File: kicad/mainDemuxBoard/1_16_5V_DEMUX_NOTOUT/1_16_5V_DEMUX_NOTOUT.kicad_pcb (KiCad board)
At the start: 4 copper layers, 168 parts, among them Q1 PMOS, Q10 PMOS, Q100 PMOS, Q101 PMOS, Q102 PMOS, Q103 PMOS, Q104 NMOS, Q105 NMOS, Q106 NMOS, Q107 NMOS, Q108 NMOS, Q109 PMOS, Q11 PMOS, Q110 PMOS, Q111 PMOS, Q112 PMOS, Q113 PMOS, Q114 NMOS, Q115 NMOS, Q116 NMOS, Q117 NMOS, Q118 NMOS, Q119 PMOS, Q12 PMOS, Q120 PMOS, Q121 PMOS, Q122 PMOS, Q123 PMOS, Q124 NMOS, Q125 NMOS, Q126 NMOS, Q127 NMOS, Q128 NMOS, Q129 PMOS, Q13 PMOS, Q130 PMOS, Q131 PMOS, Q132 PMOS, Q133 PMOS, Q134 NMOS, Q135 NMOS, Q136 NMOS, Q137 NMOS, Q138 NMOS, Q139 PMOS, Q14 NMOS, Q140 PMOS, Q141 PMOS, Q142 PMOS, Q143 PMOS, Q144 NMOS, Q145 NMOS, Q146 NMOS, Q147 NMOS, Q148 NMOS, Q149 PMOS, Q15 NMOS, Q150 PMOS, Q151 PMOS, Q152 PMOS, Q153 PMOS, Q154 NMOS, Q155 NMOS, Q156 NMOS, Q157 NMOS, Q158 NMOS, Q159 PMOS, Q16 NMOS, Q160 PMOS, Q161 PMOS, Q162 PMOS, Q163 PMOS, Q164 NMOS, Q165 NMOS, Q166 NMOS, Q167 NMOS, Q168 NMOS, Q17 NMOS, Q18 NMOS, Q19 PMOS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

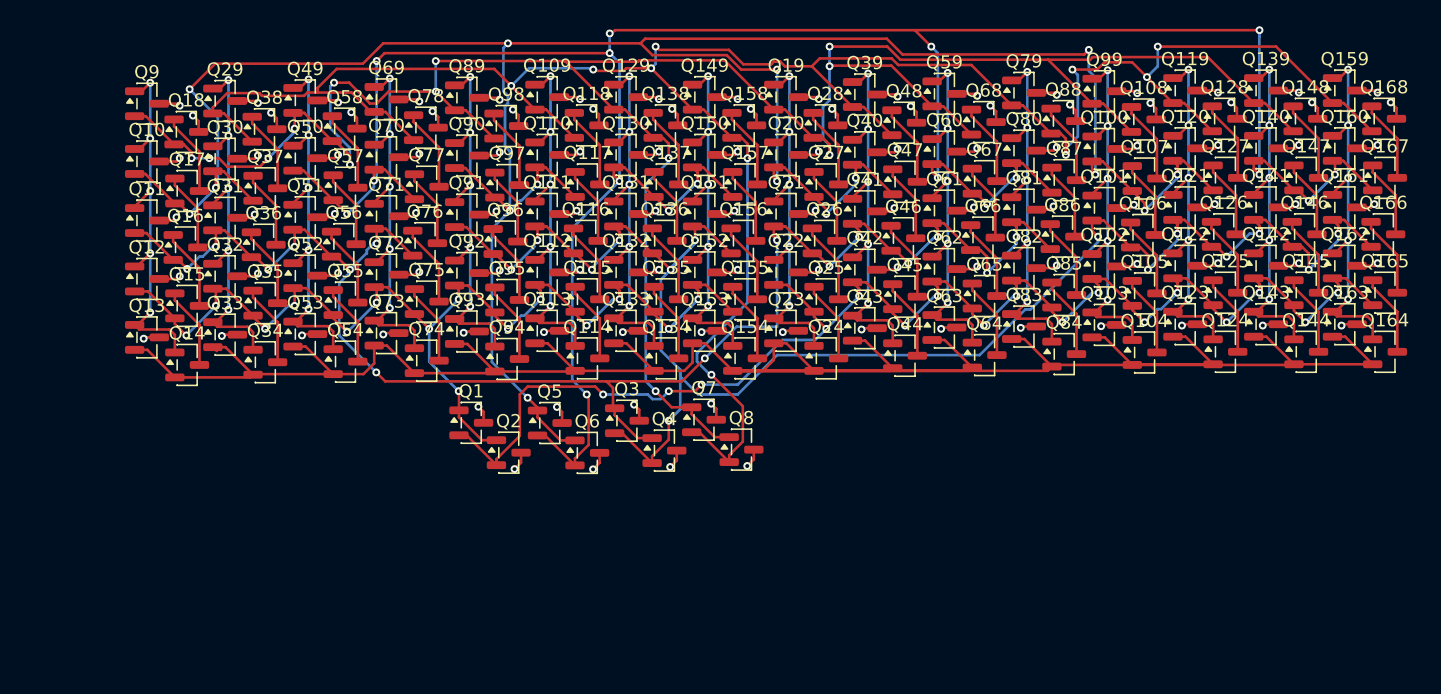
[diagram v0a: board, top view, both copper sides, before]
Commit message: update main board schematic
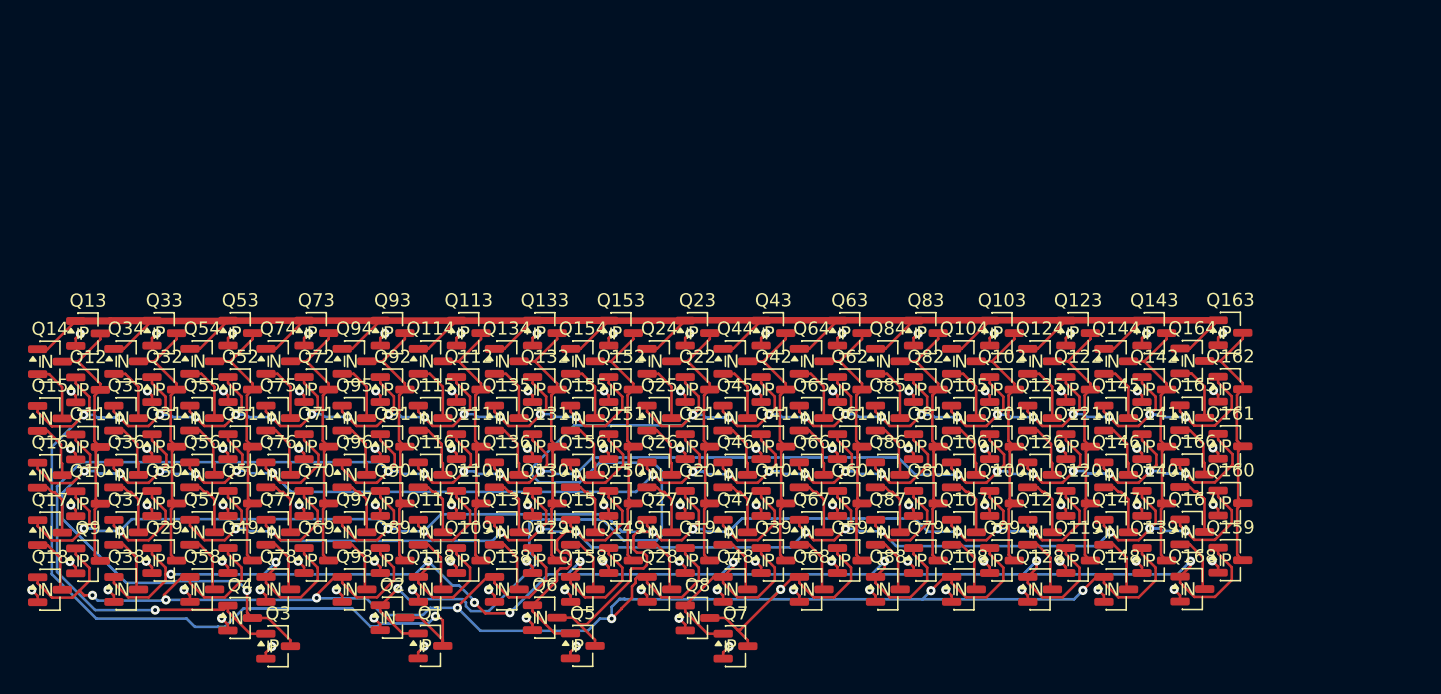
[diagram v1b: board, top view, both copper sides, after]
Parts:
- Q1, Q10, Q100, Q101, Q102, Q103, Q109, Q11, Q110, Q111, Q112, Q113, Q119, Q12, Q120, Q121, Q122, Q123, Q129, Q13, Q130, Q131, Q132, Q133, Q139, Q140, Q141, Q142, Q143, Q149, Q150, Q151, Q152, Q153, Q159, Q160, Q161, Q162, Q163, Q19, Q20, Q21, Q22, Q23, Q29, Q3, Q30, Q31, Q32, Q33, Q39, Q40, Q41, Q42, Q43, Q49, Q5, Q50, Q51, Q52, Q53, Q59, Q60, Q61, Q62, Q63, Q69, Q7, Q70, Q71, Q72, Q73, Q79, Q80, Q81, Q82, Q83, Q89, Q9, Q90, Q91, Q92, Q93, Q99: value PMOS -> Q_PMOS_GSD; footprint Package_TO_SOT_SMD:SOT-23 -> easyeda2kicad:SOT-23-P
- Q104, Q105, Q106, Q107, Q108, Q114, Q115, Q116, Q117, Q118, Q124, Q125, Q126, Q127, Q128, Q134, Q135, Q136, Q137, Q138, Q14, Q144, Q145, Q146, Q147, Q148, Q15, Q154, Q155, Q156, Q157, Q158, Q16, Q164, Q165, Q166, Q167, Q168, Q17, Q18, Q2, Q24, Q25, Q26, Q27, Q28, Q34, Q35, Q36, Q37, Q38, Q4, Q44, Q45, Q46, Q47, Q48, Q54, Q55, Q56, Q57, Q58, Q6, Q64, Q65, Q66, Q67, Q68, Q74, Q75, Q76, Q77, Q78, Q8, Q84, Q85, Q86, Q87, Q88, Q94, Q95, Q96, Q97, Q98: value NMOS -> Q_NMOS_GSD; footprint Package_TO_SOT_SMD:SOT-23 -> easyeda2kicad:SOT-23-N
- moved Q168 38.7 mm to (121.2, 128.8)
- moved Q148 38.6 mm to (115.4, 128.8)
- moved Q128 38.5 mm to (109.6, 128.8)
- moved Q108 38.3 mm to (103.8, 128.8)
- moved Q88 38.1 mm to (98.0, 128.8)
- moved Q68 37.9 mm to (92.2, 128.8)
- moved Q48 37.8 mm to (86.4, 128.8)
- moved Q28 37.5 mm to (80.6, 128.8)
- moved Q158 37.4 mm to (74.8, 128.8)
- moved Q138 37.3 mm to (69.0, 128.8)
- moved Q118 37.3 mm to (63.2, 128.8)
- moved Q98 37.1 mm to (57.4, 128.8)
- moved Q78 36.9 mm to (51.6, 128.8)
- moved Q159 36.8 mm to (124.1, 126.6)
- moved Q139 36.8 mm to (118.3, 126.7)
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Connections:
- Q1 pad 1: /5VNOT/Y -> /S_{0}
- Q1 pad 2: /S_{0} -> +5V
- Q1 pad 3: +5V -> /5VNOT/Y
- Q10 pad 1: /~{Y_{0}} -> /5VNOT2/Y
- Q10 pad 2: /5VNOT2/Y -> +5V
- Q10 pad 3: +5V -> /~{Y_{0}}
- Q100 pad 1: /~{Y_{12}} -> /5VNOT2/Y
- Q100 pad 2: /5VNOT2/Y -> +5V
- Q100 pad 3: +5V -> /~{Y_{12}}
- Q101 pad 1: /~{Y_{12}} -> /S_{1}
- Q101 pad 2: /S_{1} -> +5V
- Q101 pad 3: +5V -> /~{Y_{12}}
- Q102 pad 1: /~{Y_{12}} -> /S_{0}
- Q102 pad 2: /S_{0} -> +5V
- Q102 pad 3: +5V -> /~{Y_{12}}
- Q103 pad 1: /~{Y_{12}} -> /D
- Q103 pad 2: /D -> +5V
- Q103 pad 3: +5V -> /~{Y_{12}}
- Q104 pad 1: /~{Y_{12}} -> /D
- Q104 pad 2: /D -> Net-(Q104-S)
- Q104 pad 3: Net-(Q104-S) -> /~{Y_{12}}
- Q105 pad 1: Net-(Q104-S) -> /S_{0}
- Q105 pad 2: /S_{0} -> Net-(Q105-S)
- Q105 pad 3: Net-(Q105-S) -> Net-(Q104-S)
- Q106 pad 1: Net-(Q105-S) -> /S_{1}
- Q106 pad 2: /S_{1} -> Net-(Q106-S)
- Q106 pad 3: Net-(Q106-S) -> Net-(Q105-S)
- Q107 pad 1: Net-(Q106-S) -> /5VNOT2/Y
- Q107 pad 2: /5VNOT2/Y -> Net-(Q107-S)
- Q107 pad 3: Net-(Q107-S) -> Net-(Q106-S)
- Q108 pad 1: Net-(Q107-S) -> /5VNOT3/Y
- Q108 pad 2: /5VNOT3/Y -> GND
- Q108 pad 3: GND -> Net-(Q107-S)
- Q109 pad 1: /~{Y_{5}} -> /S_{3}
- Q109 pad 2: /S_{3} -> +5V
- Q109 pad 3: +5V -> /~{Y_{5}}
- Q11 pad 1: /~{Y_{0}} -> /5VNOT1/Y
- Q11 pad 2: /5VNOT1/Y -> +5V
- Q11 pad 3: +5V -> /~{Y_{0}}
- Q110 pad 1: /~{Y_{5}} -> /5VNOT2/Y
- Q110 pad 2: /5VNOT2/Y -> +5V
- Q110 pad 3: +5V -> /~{Y_{5}}
- Q111 pad 1: /~{Y_{5}} -> /S_{1}
- Q111 pad 2: /S_{1} -> +5V
- Q111 pad 3: +5V -> /~{Y_{5}}
- Q112 pad 1: /~{Y_{5}} -> /5VNOT/Y
- Q112 pad 2: /5VNOT/Y -> +5V
- Q112 pad 3: +5V -> /~{Y_{5}}
- Q113 pad 1: /~{Y_{5}} -> /D
- Q113 pad 2: /D -> +5V
- Q113 pad 3: +5V -> /~{Y_{5}}
- Q114 pad 1: /~{Y_{5}} -> /D
- Q114 pad 2: /D -> Net-(Q114-S)
- Q114 pad 3: Net-(Q114-S) -> /~{Y_{5}}
- Q115 pad 1: Net-(Q114-S) -> /5VNOT/Y
- Q115 pad 2: /5VNOT/Y -> Net-(Q115-S)
- Q115 pad 3: Net-(Q115-S) -> Net-(Q114-S)
- Q116 pad 1: Net-(Q115-S) -> /S_{1}
- Q116 pad 2: /S_{1} -> Net-(Q116-S)
- Q116 pad 3: Net-(Q116-S) -> Net-(Q115-S)
- Q117 pad 1: Net-(Q116-S) -> /5VNOT2/Y
- Q117 pad 2: /5VNOT2/Y -> Net-(Q117-S)
- Q117 pad 3: Net-(Q117-S) -> Net-(Q116-S)
- Q118 pad 1: Net-(Q117-S) -> /S_{3}
- Q118 pad 2: /S_{3} -> GND
- Q118 pad 3: GND -> Net-(Q117-S)
- Q119 pad 1: /~{Y_{13}} -> /S_{3}
- Q119 pad 2: /S_{3} -> +5V
- Q119 pad 3: +5V -> /~{Y_{13}}
- Q12 pad 1: /~{Y_{0}} -> /5VNOT/Y
- Q12 pad 2: /5VNOT/Y -> +5V
- Q12 pad 3: +5V -> /~{Y_{0}}
- Q120 pad 1: /~{Y_{13}} -> /5VNOT2/Y
- Q120 pad 2: /5VNOT2/Y -> +5V
- Q120 pad 3: +5V -> /~{Y_{13}}
- Q121 pad 1: /~{Y_{13}} -> /S_{1}
- Q121 pad 2: /S_{1} -> +5V
- Q121 pad 3: +5V -> /~{Y_{13}}
- Q122 pad 1: /~{Y_{13}} -> /S_{0}
- Q122 pad 2: /S_{0} -> +5V
- Q122 pad 3: +5V -> /~{Y_{13}}
- Q123 pad 1: /~{Y_{13}} -> /D
- Q123 pad 2: /D -> +5V
- Q123 pad 3: +5V -> /~{Y_{13}}
- Q124 pad 1: /~{Y_{13}} -> /D
- Q124 pad 2: /D -> Net-(Q124-S)
- Q124 pad 3: Net-(Q124-S) -> /~{Y_{13}}
- Q125 pad 1: Net-(Q124-S) -> /S_{0}
- Q125 pad 2: /S_{0} -> Net-(Q125-S)
- Q125 pad 3: Net-(Q125-S) -> Net-(Q124-S)
- Q126 pad 1: Net-(Q125-S) -> /S_{1}
- Q126 pad 2: /S_{1} -> Net-(Q126-S)
- Q126 pad 3: Net-(Q126-S) -> Net-(Q125-S)
- Q127 pad 1: Net-(Q126-S) -> /5VNOT2/Y
- Q127 pad 2: /5VNOT2/Y -> Net-(Q127-S)
- Q127 pad 3: Net-(Q127-S) -> Net-(Q126-S)
- Q128 pad 1: Net-(Q127-S) -> /S_{3}
- Q128 pad 2: /S_{3} -> GND
- Q128 pad 3: GND -> Net-(Q127-S)
- Q129 pad 1: /~{Y_{6}} -> /5VNOT3/Y
- Q129 pad 2: /5VNOT3/Y -> +5V
- Q129 pad 3: +5V -> /~{Y_{6}}
- Q13 pad 1: /~{Y_{0}} -> /D
- Q13 pad 2: /D -> +5V
- Q13 pad 3: +5V -> /~{Y_{0}}
- Q130 pad 1: /~{Y_{6}} -> /S_{2}
- Q130 pad 2: /S_{2} -> +5V
- Q130 pad 3: +5V -> /~{Y_{6}}
- Q131 pad 1: /~{Y_{6}} -> /S_{1}
- Q131 pad 2: /S_{1} -> +5V
- Q131 pad 3: +5V -> /~{Y_{6}}
- Q132 pad 1: /~{Y_{6}} -> /5VNOT/Y
- Q132 pad 2: /5VNOT/Y -> +5V
- Q132 pad 3: +5V -> /~{Y_{6}}
- Q133 pad 1: /~{Y_{6}} -> /D
- Q133 pad 2: /D -> +5V
- Q133 pad 3: +5V -> /~{Y_{6}}
- Q134 pad 1: /~{Y_{6}} -> /D
- Q134 pad 2: /D -> Net-(Q134-S)
- Q134 pad 3: Net-(Q134-S) -> /~{Y_{6}}
- Q135 pad 1: Net-(Q134-S) -> /5VNOT/Y
- Q135 pad 2: /5VNOT/Y -> Net-(Q135-S)
- Q135 pad 3: Net-(Q135-S) -> Net-(Q134-S)
- Q136 pad 1: Net-(Q135-S) -> /S_{1}
- Q136 pad 2: /S_{1} -> Net-(Q136-S)
- Q136 pad 3: Net-(Q136-S) -> Net-(Q135-S)
- Q137 pad 1: Net-(Q136-S) -> /S_{2}
- Q137 pad 2: /S_{2} -> Net-(Q137-S)
- Q137 pad 3: Net-(Q137-S) -> Net-(Q136-S)
- Q138 pad 1: Net-(Q137-S) -> /5VNOT3/Y
- Q138 pad 2: /5VNOT3/Y -> GND
- Q138 pad 3: GND -> Net-(Q137-S)
- Q139 pad 1: /~{Y_{14}} -> /5VNOT3/Y
- Q139 pad 2: /5VNOT3/Y -> +5V
- Q139 pad 3: +5V -> /~{Y_{14}}
- Q14 pad 1: /~{Y_{0}} -> /D
- Q14 pad 2: /D -> Net-(Q14-S)
- Q14 pad 3: Net-(Q14-S) -> /~{Y_{0}}
- Q140 pad 1: /~{Y_{14}} -> /S_{2}
- Q140 pad 2: /S_{2} -> +5V
- Q140 pad 3: +5V -> /~{Y_{14}}
- Q141 pad 1: /~{Y_{14}} -> /S_{1}
- Q141 pad 2: /S_{1} -> +5V
- Q141 pad 3: +5V -> /~{Y_{14}}
- Q142 pad 1: /~{Y_{14}} -> /S_{0}
- Q142 pad 2: /S_{0} -> +5V
- Q142 pad 3: +5V -> /~{Y_{14}}
- Q143 pad 1: /~{Y_{14}} -> /D
- Q143 pad 2: /D -> +5V
- Q143 pad 3: +5V -> /~{Y_{14}}
- Q144 pad 1: /~{Y_{14}} -> /D
- Q144 pad 2: /D -> Net-(Q144-S)
- Q144 pad 3: Net-(Q144-S) -> /~{Y_{14}}
- Q145 pad 1: Net-(Q144-S) -> /S_{0}
- Q145 pad 2: /S_{0} -> Net-(Q145-S)
- Q145 pad 3: Net-(Q145-S) -> Net-(Q144-S)
- Q146 pad 1: Net-(Q145-S) -> /S_{1}
- Q146 pad 2: /S_{1} -> Net-(Q146-S)
- Q146 pad 3: Net-(Q146-S) -> Net-(Q145-S)
- Q147 pad 1: Net-(Q146-S) -> /S_{2}
- Q147 pad 2: /S_{2} -> Net-(Q147-S)
- Q147 pad 3: Net-(Q147-S) -> Net-(Q146-S)
- Q148 pad 1: Net-(Q147-S) -> /5VNOT3/Y
- Q148 pad 2: /5VNOT3/Y -> GND
- Q148 pad 3: GND -> Net-(Q147-S)
- Q149 pad 1: /~{Y_{7}} -> /S_{3}
- Q149 pad 2: /S_{3} -> +5V
- Q149 pad 3: +5V -> /~{Y_{7}}
- Q15 pad 1: Net-(Q14-S) -> /5VNOT/Y
- Q15 pad 2: /5VNOT/Y -> Net-(Q15-S)
- Q15 pad 3: Net-(Q15-S) -> Net-(Q14-S)
- Q150 pad 1: /~{Y_{7}} -> /S_{2}
- Q150 pad 2: /S_{2} -> +5V
- Q150 pad 3: +5V -> /~{Y_{7}}
- Q151 pad 1: /~{Y_{7}} -> /S_{1}
- Q151 pad 2: /S_{1} -> +5V
- Q151 pad 3: +5V -> /~{Y_{7}}
- Q152 pad 1: /~{Y_{7}} -> /5VNOT/Y
- Q152 pad 2: /5VNOT/Y -> +5V
- Q152 pad 3: +5V -> /~{Y_{7}}
- Q153 pad 1: /~{Y_{7}} -> /D
- Q153 pad 2: /D -> +5V
- Q153 pad 3: +5V -> /~{Y_{7}}
- Q154 pad 1: /~{Y_{7}} -> /D
- Q154 pad 2: /D -> Net-(Q154-S)
- Q154 pad 3: Net-(Q154-S) -> /~{Y_{7}}
- Q155 pad 1: Net-(Q154-S) -> /5VNOT/Y
- Q155 pad 2: /5VNOT/Y -> Net-(Q155-S)
- Q155 pad 3: Net-(Q155-S) -> Net-(Q154-S)
- Q156 pad 1: Net-(Q155-S) -> /S_{1}
- Q156 pad 2: /S_{1} -> Net-(Q156-S)
- Q156 pad 3: Net-(Q156-S) -> Net-(Q155-S)
- Q157 pad 1: Net-(Q156-S) -> /S_{2}
- Q157 pad 2: /S_{2} -> Net-(Q157-S)
- Q157 pad 3: Net-(Q157-S) -> Net-(Q156-S)
- Q158 pad 1: Net-(Q157-S) -> /S_{3}
- Q158 pad 2: /S_{3} -> GND
- Q158 pad 3: GND -> Net-(Q157-S)
- Q159 pad 1: /~{Y_{15}} -> /S_{3}
- Q159 pad 2: /S_{3} -> +5V
- Q159 pad 3: +5V -> /~{Y_{15}}
- Q16 pad 1: Net-(Q15-S) -> /5VNOT1/Y
- Q16 pad 2: /5VNOT1/Y -> Net-(Q16-S)
- Q16 pad 3: Net-(Q16-S) -> Net-(Q15-S)
- Q160 pad 1: /~{Y_{15}} -> /S_{2}
- Q160 pad 2: /S_{2} -> +5V
- Q160 pad 3: +5V -> /~{Y_{15}}
- Q161 pad 1: /~{Y_{15}} -> /S_{1}
- Q161 pad 2: /S_{1} -> +5V
- Q161 pad 3: +5V -> /~{Y_{15}}
- Q162 pad 1: /~{Y_{15}} -> /S_{0}
- Q162 pad 2: /S_{0} -> +5V
- Q162 pad 3: +5V -> /~{Y_{15}}
- Q163 pad 1: /~{Y_{15}} -> /D
- Q163 pad 2: /D -> +5V
- Q163 pad 3: +5V -> /~{Y_{15}}
- Q164 pad 1: /~{Y_{15}} -> /D
- Q164 pad 2: /D -> Net-(Q164-S)
- Q164 pad 3: Net-(Q164-S) -> /~{Y_{15}}
- Q165 pad 1: Net-(Q164-S) -> /S_{0}
- Q165 pad 2: /S_{0} -> Net-(Q165-S)
- Q165 pad 3: Net-(Q165-S) -> Net-(Q164-S)
- Q166 pad 1: Net-(Q165-S) -> /S_{1}
- Q166 pad 2: /S_{1} -> Net-(Q166-S)
- Q166 pad 3: Net-(Q166-S) -> Net-(Q165-S)
- Q167 pad 1: Net-(Q166-S) -> /S_{2}
- Q167 pad 2: /S_{2} -> Net-(Q167-S)
- Q167 pad 3: Net-(Q167-S) -> Net-(Q166-S)
- Q168 pad 1: Net-(Q167-S) -> /S_{3}
- Q168 pad 2: /S_{3} -> GND
- Q168 pad 3: GND -> Net-(Q167-S)
- Q17 pad 1: Net-(Q16-S) -> /5VNOT2/Y
- Q17 pad 2: /5VNOT2/Y -> Net-(Q17-S)
- Q17 pad 3: Net-(Q17-S) -> Net-(Q16-S)
- Q18 pad 1: Net-(Q17-S) -> /5VNOT3/Y
- Q18 pad 2: /5VNOT3/Y -> GND
- Q18 pad 3: GND -> Net-(Q17-S)
- Q19 pad 1: /~{Y_{8}} -> /5VNOT3/Y
- Q19 pad 2: /5VNOT3/Y -> +5V
- Q19 pad 3: +5V -> /~{Y_{8}}
- Q2 pad 1: /5VNOT/Y -> /S_{0}
- Q2 pad 2: /S_{0} -> GND
- Q2 pad 3: GND -> /5VNOT/Y
- Q20 pad 1: /~{Y_{8}} -> /5VNOT2/Y
- Q20 pad 2: /5VNOT2/Y -> +5V
- Q20 pad 3: +5V -> /~{Y_{8}}
- Q21 pad 1: /~{Y_{8}} -> /5VNOT1/Y
- Q21 pad 2: /5VNOT1/Y -> +5V
- Q21 pad 3: +5V -> /~{Y_{8}}
- Q22 pad 1: /~{Y_{8}} -> /S_{0}
- Q22 pad 2: /S_{0} -> +5V
- Q22 pad 3: +5V -> /~{Y_{8}}
- Q23 pad 1: /~{Y_{8}} -> /D
- Q23 pad 2: /D -> +5V
- Q23 pad 3: +5V -> /~{Y_{8}}
- Q24 pad 1: /~{Y_{8}} -> /D
- Q24 pad 2: /D -> Net-(Q24-S)
- Q24 pad 3: Net-(Q24-S) -> /~{Y_{8}}
- Q25 pad 1: Net-(Q24-S) -> /S_{0}
- Q25 pad 2: /S_{0} -> Net-(Q25-S)
- Q25 pad 3: Net-(Q25-S) -> Net-(Q24-S)
- Q26 pad 1: Net-(Q25-S) -> /5VNOT1/Y
- Q26 pad 2: /5VNOT1/Y -> Net-(Q26-S)
- Q26 pad 3: Net-(Q26-S) -> Net-(Q25-S)
- Q27 pad 1: Net-(Q26-S) -> /5VNOT2/Y
- Q27 pad 2: /5VNOT2/Y -> Net-(Q27-S)
- Q27 pad 3: Net-(Q27-S) -> Net-(Q26-S)
- Q28 pad 1: Net-(Q27-S) -> /5VNOT3/Y
- Q28 pad 2: /5VNOT3/Y -> GND
- Q28 pad 3: GND -> Net-(Q27-S)
- Q29 pad 1: /~{Y_{1}} -> /S_{3}
- Q29 pad 2: /S_{3} -> +5V
- Q29 pad 3: +5V -> /~{Y_{1}}
- Q3 pad 1: /5VNOT1/Y -> /S_{1}
- Q3 pad 2: /S_{1} -> +5V
- Q3 pad 3: +5V -> /5VNOT1/Y
- Q30 pad 1: /~{Y_{1}} -> /5VNOT2/Y
- Q30 pad 2: /5VNOT2/Y -> +5V
- Q30 pad 3: +5V -> /~{Y_{1}}
- Q31 pad 1: /~{Y_{1}} -> /5VNOT1/Y
- Q31 pad 2: /5VNOT1/Y -> +5V
- Q31 pad 3: +5V -> /~{Y_{1}}
- Q32 pad 1: /~{Y_{1}} -> /5VNOT/Y
- Q32 pad 2: /5VNOT/Y -> +5V
- Q32 pad 3: +5V -> /~{Y_{1}}
- Q33 pad 1: /~{Y_{1}} -> /D
- Q33 pad 2: /D -> +5V
- Q33 pad 3: +5V -> /~{Y_{1}}
- Q34 pad 1: /~{Y_{1}} -> /D
- Q34 pad 2: /D -> Net-(Q34-S)
- Q34 pad 3: Net-(Q34-S) -> /~{Y_{1}}
- Q35 pad 1: Net-(Q34-S) -> /5VNOT/Y
- Q35 pad 2: /5VNOT/Y -> Net-(Q35-S)
- Q35 pad 3: Net-(Q35-S) -> Net-(Q34-S)
- Q36 pad 1: Net-(Q35-S) -> /5VNOT1/Y
- Q36 pad 2: /5VNOT1/Y -> Net-(Q36-S)
- Q36 pad 3: Net-(Q36-S) -> Net-(Q35-S)
- Q37 pad 1: Net-(Q36-S) -> /5VNOT2/Y
- Q37 pad 2: /5VNOT2/Y -> Net-(Q37-S)
- Q37 pad 3: Net-(Q37-S) -> Net-(Q36-S)
- Q38 pad 1: Net-(Q37-S) -> /S_{3}
- Q38 pad 2: /S_{3} -> GND
- Q38 pad 3: GND -> Net-(Q37-S)
- Q39 pad 1: /~{Y_{9}} -> /S_{3}
- Q39 pad 2: /S_{3} -> +5V
- Q39 pad 3: +5V -> /~{Y_{9}}
- Q4 pad 1: /5VNOT1/Y -> /S_{1}
- Q4 pad 2: /S_{1} -> GND
- Q4 pad 3: GND -> /5VNOT1/Y
- Q40 pad 1: /~{Y_{9}} -> /5VNOT2/Y
- Q40 pad 2: /5VNOT2/Y -> +5V
- Q40 pad 3: +5V -> /~{Y_{9}}
- Q41 pad 1: /~{Y_{9}} -> /5VNOT1/Y
- Q41 pad 2: /5VNOT1/Y -> +5V
- Q41 pad 3: +5V -> /~{Y_{9}}
- Q42 pad 1: /~{Y_{9}} -> /S_{0}
- Q42 pad 2: /S_{0} -> +5V
- Q42 pad 3: +5V -> /~{Y_{9}}
- Q43 pad 1: /~{Y_{9}} -> /D
- Q43 pad 2: /D -> +5V
- Q43 pad 3: +5V -> /~{Y_{9}}
- Q44 pad 1: /~{Y_{9}} -> /D
- Q44 pad 2: /D -> Net-(Q44-S)
- Q44 pad 3: Net-(Q44-S) -> /~{Y_{9}}
- Q45 pad 1: Net-(Q44-S) -> /S_{0}
- Q45 pad 2: /S_{0} -> Net-(Q45-S)
- Q45 pad 3: Net-(Q45-S) -> Net-(Q44-S)
- Q46 pad 1: Net-(Q45-S) -> /5VNOT1/Y
- Q46 pad 2: /5VNOT1/Y -> Net-(Q46-S)
- Q46 pad 3: Net-(Q46-S) -> Net-(Q45-S)
- Q47 pad 1: Net-(Q46-S) -> /5VNOT2/Y
- Q47 pad 2: /5VNOT2/Y -> Net-(Q47-S)
- Q47 pad 3: Net-(Q47-S) -> Net-(Q46-S)
- Q48 pad 1: Net-(Q47-S) -> /S_{3}
- Q48 pad 2: /S_{3} -> GND
- Q48 pad 3: GND -> Net-(Q47-S)
- Q49 pad 1: /~{Y_{2}} -> /5VNOT3/Y
- Q49 pad 2: /5VNOT3/Y -> +5V
- Q49 pad 3: +5V -> /~{Y_{2}}
- Q5 pad 1: /5VNOT2/Y -> /S_{2}
- Q5 pad 2: /S_{2} -> +5V
- Q5 pad 3: +5V -> /5VNOT2/Y
- Q50 pad 1: /~{Y_{2}} -> /S_{2}
- Q50 pad 2: /S_{2} -> +5V
- Q50 pad 3: +5V -> /~{Y_{2}}
- Q51 pad 1: /~{Y_{2}} -> /5VNOT1/Y
- Q51 pad 2: /5VNOT1/Y -> +5V
- Q51 pad 3: +5V -> /~{Y_{2}}
- Q52 pad 1: /~{Y_{2}} -> /5VNOT/Y
- Q52 pad 2: /5VNOT/Y -> +5V
- Q52 pad 3: +5V -> /~{Y_{2}}
- Q53 pad 1: /~{Y_{2}} -> /D
- Q53 pad 2: /D -> +5V
- Q53 pad 3: +5V -> /~{Y_{2}}
- Q54 pad 1: /~{Y_{2}} -> /D
- Q54 pad 2: /D -> Net-(Q54-S)
- Q54 pad 3: Net-(Q54-S) -> /~{Y_{2}}
- Q55 pad 1: Net-(Q54-S) -> /5VNOT/Y
- Q55 pad 2: /5VNOT/Y -> Net-(Q55-S)
- Q55 pad 3: Net-(Q55-S) -> Net-(Q54-S)
- Q56 pad 1: Net-(Q55-S) -> /5VNOT1/Y
- Q56 pad 2: /5VNOT1/Y -> Net-(Q56-S)
- Q56 pad 3: Net-(Q56-S) -> Net-(Q55-S)
- Q57 pad 1: Net-(Q56-S) -> /S_{2}
- Q57 pad 2: /S_{2} -> Net-(Q57-S)
- Q57 pad 3: Net-(Q57-S) -> Net-(Q56-S)
- Q58 pad 1: Net-(Q57-S) -> /5VNOT3/Y
- Q58 pad 2: /5VNOT3/Y -> GND
- Q58 pad 3: GND -> Net-(Q57-S)
- Q59 pad 1: /~{Y_{10}} -> /5VNOT3/Y
- Q59 pad 2: /5VNOT3/Y -> +5V
- Q59 pad 3: +5V -> /~{Y_{10}}
- Q6 pad 1: /5VNOT2/Y -> /S_{2}
- Q6 pad 2: /S_{2} -> GND
- Q6 pad 3: GND -> /5VNOT2/Y
- Q60 pad 1: /~{Y_{10}} -> /S_{2}
- Q60 pad 2: /S_{2} -> +5V
- Q60 pad 3: +5V -> /~{Y_{10}}
- Q61 pad 1: /~{Y_{10}} -> /5VNOT1/Y
- Q61 pad 2: /5VNOT1/Y -> +5V
- Q61 pad 3: +5V -> /~{Y_{10}}
- Q62 pad 1: /~{Y_{10}} -> /S_{0}
- Q62 pad 2: /S_{0} -> +5V
- Q62 pad 3: +5V -> /~{Y_{10}}
- Q63 pad 1: /~{Y_{10}} -> /D
- Q63 pad 2: /D -> +5V
- Q63 pad 3: +5V -> /~{Y_{10}}
- Q64 pad 1: /~{Y_{10}} -> /D
- Q64 pad 2: /D -> Net-(Q64-S)
- Q64 pad 3: Net-(Q64-S) -> /~{Y_{10}}
- Q65 pad 1: Net-(Q64-S) -> /S_{0}
- Q65 pad 2: /S_{0} -> Net-(Q65-S)
- Q65 pad 3: Net-(Q65-S) -> Net-(Q64-S)
- Q66 pad 1: Net-(Q65-S) -> /5VNOT1/Y
- Q66 pad 2: /5VNOT1/Y -> Net-(Q66-S)
- Q66 pad 3: Net-(Q66-S) -> Net-(Q65-S)
- Q67 pad 1: Net-(Q66-S) -> /S_{2}
- Q67 pad 2: /S_{2} -> Net-(Q67-S)
- Q67 pad 3: Net-(Q67-S) -> Net-(Q66-S)
- Q68 pad 1: Net-(Q67-S) -> /5VNOT3/Y
- Q68 pad 2: /5VNOT3/Y -> GND
- Q68 pad 3: GND -> Net-(Q67-S)
- Q69 pad 1: /~{Y_{3}} -> /S_{3}
- Q69 pad 2: /S_{3} -> +5V
- Q69 pad 3: +5V -> /~{Y_{3}}
- Q7 pad 1: /5VNOT3/Y -> /S_{3}
- Q7 pad 2: /S_{3} -> +5V
- Q7 pad 3: +5V -> /5VNOT3/Y
- Q70 pad 1: /~{Y_{3}} -> /S_{2}
- Q70 pad 2: /S_{2} -> +5V
- Q70 pad 3: +5V -> /~{Y_{3}}
- Q71 pad 1: /~{Y_{3}} -> /5VNOT1/Y
- Q71 pad 2: /5VNOT1/Y -> +5V
- Q71 pad 3: +5V -> /~{Y_{3}}
- Q72 pad 1: /~{Y_{3}} -> /5VNOT/Y
- Q72 pad 2: /5VNOT/Y -> +5V
- Q72 pad 3: +5V -> /~{Y_{3}}
- Q73 pad 1: /~{Y_{3}} -> /D
- Q73 pad 2: /D -> +5V
- Q73 pad 3: +5V -> /~{Y_{3}}
- Q74 pad 1: /~{Y_{3}} -> /D
- Q74 pad 2: /D -> Net-(Q74-S)
- Q74 pad 3: Net-(Q74-S) -> /~{Y_{3}}
- Q75 pad 1: Net-(Q74-S) -> /5VNOT/Y
- Q75 pad 2: /5VNOT/Y -> Net-(Q75-S)
- Q75 pad 3: Net-(Q75-S) -> Net-(Q74-S)
- Q76 pad 1: Net-(Q75-S) -> /5VNOT1/Y
- Q76 pad 2: /5VNOT1/Y -> Net-(Q76-S)
- Q76 pad 3: Net-(Q76-S) -> Net-(Q75-S)
- Q77 pad 1: Net-(Q76-S) -> /S_{2}
- Q77 pad 2: /S_{2} -> Net-(Q77-S)
- Q77 pad 3: Net-(Q77-S) -> Net-(Q76-S)
- Q78 pad 1: Net-(Q77-S) -> /S_{3}
- Q78 pad 2: /S_{3} -> GND
- Q78 pad 3: GND -> Net-(Q77-S)
- Q79 pad 1: /~{Y_{11}} -> /S_{3}
- Q79 pad 2: /S_{3} -> +5V
- Q79 pad 3: +5V -> /~{Y_{11}}
- Q8 pad 1: /5VNOT3/Y -> /S_{3}
- Q8 pad 2: /S_{3} -> GND
- Q8 pad 3: GND -> /5VNOT3/Y
- Q80 pad 1: /~{Y_{11}} -> /S_{2}
- Q80 pad 2: /S_{2} -> +5V
- Q80 pad 3: +5V -> /~{Y_{11}}
- Q81 pad 1: /~{Y_{11}} -> /5VNOT1/Y
- Q81 pad 2: /5VNOT1/Y -> +5V
- Q81 pad 3: +5V -> /~{Y_{11}}
- Q82 pad 1: /~{Y_{11}} -> /S_{0}
- Q82 pad 2: /S_{0} -> +5V
- Q82 pad 3: +5V -> /~{Y_{11}}
- Q83 pad 1: /~{Y_{11}} -> /D
- Q83 pad 2: /D -> +5V
- Q83 pad 3: +5V -> /~{Y_{11}}
- Q84 pad 1: /~{Y_{11}} -> /D
- Q84 pad 2: /D -> Net-(Q84-S)
- Q84 pad 3: Net-(Q84-S) -> /~{Y_{11}}
- Q85 pad 1: Net-(Q84-S) -> /S_{0}
- Q85 pad 2: /S_{0} -> Net-(Q85-S)
- Q85 pad 3: Net-(Q85-S) -> Net-(Q84-S)
- Q86 pad 1: Net-(Q85-S) -> /5VNOT1/Y
- Q86 pad 2: /5VNOT1/Y -> Net-(Q86-S)
- Q86 pad 3: Net-(Q86-S) -> Net-(Q85-S)
- Q87 pad 1: Net-(Q86-S) -> /S_{2}
- Q87 pad 2: /S_{2} -> Net-(Q87-S)
- Q87 pad 3: Net-(Q87-S) -> Net-(Q86-S)
- Q88 pad 1: Net-(Q87-S) -> /S_{3}
- Q88 pad 2: /S_{3} -> GND
- Q88 pad 3: GND -> Net-(Q87-S)
- Q89 pad 1: /~{Y_{4}} -> /5VNOT3/Y
- Q89 pad 2: /5VNOT3/Y -> +5V
- Q89 pad 3: +5V -> /~{Y_{4}}
- Q9 pad 1: /~{Y_{0}} -> /5VNOT3/Y
- Q9 pad 2: /5VNOT3/Y -> +5V
- Q9 pad 3: +5V -> /~{Y_{0}}
- Q90 pad 1: /~{Y_{4}} -> /5VNOT2/Y
- Q90 pad 2: /5VNOT2/Y -> +5V
- Q90 pad 3: +5V -> /~{Y_{4}}
- Q91 pad 1: /~{Y_{4}} -> /S_{1}
- Q91 pad 2: /S_{1} -> +5V
- Q91 pad 3: +5V -> /~{Y_{4}}
- Q92 pad 1: /~{Y_{4}} -> /5VNOT/Y
- Q92 pad 2: /5VNOT/Y -> +5V
- Q92 pad 3: +5V -> /~{Y_{4}}
- Q93 pad 1: /~{Y_{4}} -> /D
- Q93 pad 2: /D -> +5V
- Q93 pad 3: +5V -> /~{Y_{4}}
- Q94 pad 1: /~{Y_{4}} -> /D
- Q94 pad 2: /D -> Net-(Q94-S)
- Q94 pad 3: Net-(Q94-S) -> /~{Y_{4}}
- Q95 pad 1: Net-(Q94-S) -> /5VNOT/Y
- Q95 pad 2: /5VNOT/Y -> Net-(Q95-S)
- Q95 pad 3: Net-(Q95-S) -> Net-(Q94-S)
- Q96 pad 1: Net-(Q95-S) -> /S_{1}
- Q96 pad 2: /S_{1} -> Net-(Q96-S)
- Q96 pad 3: Net-(Q96-S) -> Net-(Q95-S)
- Q97 pad 1: Net-(Q96-S) -> /5VNOT2/Y
- Q97 pad 2: /5VNOT2/Y -> Net-(Q97-S)
- Q97 pad 3: Net-(Q97-S) -> Net-(Q96-S)
- Q98 pad 1: Net-(Q97-S) -> /5VNOT3/Y
- Q98 pad 2: /5VNOT3/Y -> GND
- Q98 pad 3: GND -> Net-(Q97-S)
- Q99 pad 1: /~{Y_{12}} -> /5VNOT3/Y
- Q99 pad 2: /5VNOT3/Y -> +5V
- Q99 pad 3: +5V -> /~{Y_{12}}
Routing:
- net /S_{2}: track 198.1 -> 145.3 mm, vias 17 -> 11
- net /5VNOT/Y: track 85.3 -> 137.9 mm
- net /5VNOT2/Y: track 202.3 -> 151.4 mm, vias 15 -> 10
- net /D: track 200.0 -> 159.3 mm
- net +5V: track 126.8 -> 86.8 mm
- net /S_{0}: track 112.2 -> 149.2 mm, vias 17 -> 15
- net /S_{1}: track 129.7 -> 164.4 mm
- net /5VNOT1/Y: track 123.4 -> 140.3 mm, vias 15 -> 14
- net /S_{3}: track 184.8 -> 173.1 mm
- net /5VNOT3/Y: track 187.0 -> 177.7 mm, vias 13 -> 8
- net /~{Y_{10}}: track 30.2 -> 20.9 mm, vias 5 -> 0
- net /~{Y_{9}}: track 30.2 -> 20.9 mm, vias 5 -> 0
- net /~{Y_{15}}: track 30.2 -> 20.9 mm, vias 5 -> 0
- net /~{Y_{7}}: track 30.2 -> 20.9 mm, vias 5 -> 0
- net /~{Y_{2}}: track 30.2 -> 20.9 mm, vias 5 -> 0
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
